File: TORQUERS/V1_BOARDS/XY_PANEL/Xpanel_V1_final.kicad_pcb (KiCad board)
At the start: 4 copper layers, 82.6 x 98 mm, 97 parts, among them J1 F3311A7H121014E200, J2 F3311A7H121014E200, Q1 BSS138, Q10 MBT2222ADW1T1, Q11 BSS138, Q12 MBT2222ADW1T1, Q2 BSS138, Q3 BSS138, Q4 MBT2222ADW1T1, Q5 BSS138, Q6 MBT2222ADW1T1, Q7 BSS138, Q8 BSS138, Q9 BSS138, U1 LTC3130EUDC-1-PBF, U2 DRV8830DGQ, U3 OPT4001DTST, U4 LTC3130EUDC-1-PBF

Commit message: made changes according to feedback
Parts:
- added locked: CL21A106KOQNNNE, AA_AUTO_LOADER:CAPC2012X140N, B.Cu at (147.0, 94.5)
- locked: renamed from R23; value 0 -> locked
- locked: renamed from Q7; value BSS138 -> locked
- locked: renamed from R18; value 10K -> locked
- locked: renamed from D7; value B220 -> locked
- locked: renamed from Q11; value BSS138 -> locked
- locked: renamed from C10; value 10nF -> locked
- locked: renamed from C13; value 10nF -> locked
- locked: renamed from R5; value 0 -> locked
- locked: renamed from U1; value LTC3130EUDC-1-PBF -> locked
- locked: renamed from R3; value 0 -> locked
- locked: renamed from D5; value B220 -> locked
- locked: renamed from R33; value 10K -> locked
- locked: renamed from R25; value 10K -> locked
- locked: renamed from C11; value 10nF -> locked
- locked: renamed from R31; value 10K -> locked
- locked: renamed from C12; value 10nF -> locked
- locked: renamed from JP4; value ~ -> locked
- locked: renamed from R29; value 10K -> locked
- locked: renamed from R37; value 10K -> locked
- locked: renamed from R38; value 100K -> locked
- locked: renamed from Q8; value BSS138 -> locked
- locked: renamed from R24; value 10K -> locked
- locked: renamed from R30; value 600 -> locked
- locked: renamed from R22; value 0 -> locked
- locked: renamed from R35; value 600 -> locked
- locked: renamed from R32; value 10K -> locked
- locked: renamed from R11; value 0 -> locked
- locked: renamed from R28; value 0 -> locked
- locked: renamed from R15; value 10K -> locked
- locked: renamed from R2; value 0 -> locked
- locked: renamed from Q9; value BSS138 -> locked
- locked: renamed from U4; value LTC3130EUDC-1-PBF -> locked
- locked: renamed from Q2; value BSS138 -> locked
- locked: renamed from Q3; value BSS138 -> locked
- locked: renamed from R27; value 0 -> locked
- locked: renamed from Q1; value BSS138 -> locked
- locked: renamed from R1; value 0 -> locked
- locked: renamed from D4; value B220 -> locked
- locked: renamed from R12; value 0 -> locked
- locked: renamed from R6; value 0 -> locked
- locked: renamed from R34; value 100K -> locked
- locked: renamed from D8; value B220 -> locked
- locked: renamed from JP3; value ~ -> locked
- locked: renamed from R10; value 0 -> locked
- locked: renamed from R21; value 600 -> locked
- locked: renamed from R4; value 0 -> locked
- locked: renamed from Q6; value MBT2222ADW1T1 -> locked
- locked: renamed from Q10; value MBT2222ADW1T1 -> locked
- locked: renamed from C6; value 10uF -> locked
- locked: renamed from R26; value 100K -> locked
- locked: renamed from Q5; value BSS138 -> locked
- locked: renamed from R7; value 0 -> locked
- locked: renamed from R36; value 10K -> locked
- locked: renamed from R16; value 600 -> locked
- locked: renamed from R17; value 10K -> locked
- locked: renamed from R19; value 10K -> locked
- locked: renamed from Q4; value MBT2222ADW1T1 -> locked
- locked: renamed from U2; value DRV8830DGQ -> locked
- locked: renamed from Q12; value MBT2222ADW1T1 -> locked
- locked: renamed from R20; value 100K -> locked
- locked: renamed from C8; value 0.1uF -> locked
- renumbered S1 to locked, R40 to locked, C19 to locked, L3 to locked, R9 to locked, C7 to locked, R8 to locked, C3 to locked, C17 to locked, R42 to locked, C15 to locked, J1 to locked, R13 to locked, C18 to locked, C1 to locked, R41 to locked, R39 to locked, L4 to locked, C16 to locked, C14 to locked, R14 to locked, C4 to locked, C9 to locked, C5 to locked
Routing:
- net Net-(D4-K): track 21.1 -> 23.7 mm
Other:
- board text added: "ARGUS_1 XY"
- board text added: "locked"
- board text removed: "XY SIDE PANEL BOARD ARGUS1 REV1.0"

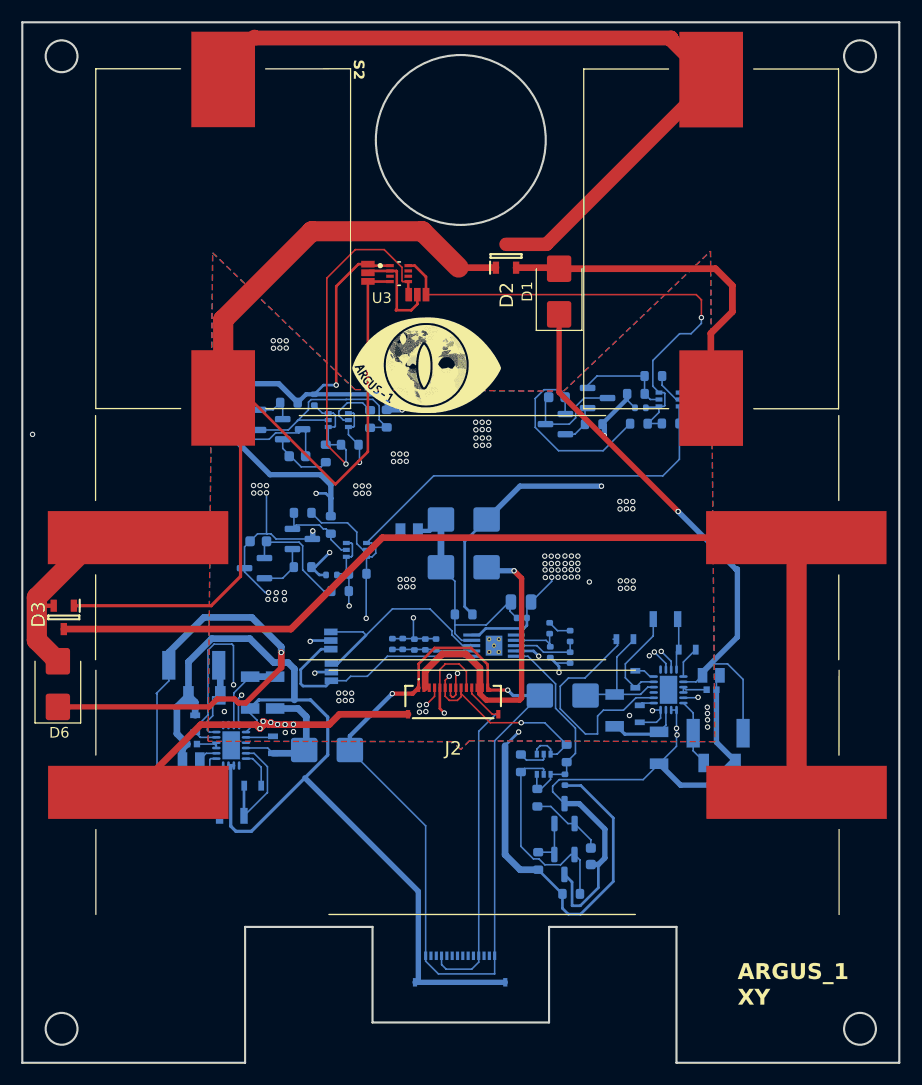
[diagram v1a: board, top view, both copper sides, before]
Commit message: added buck for coil driver
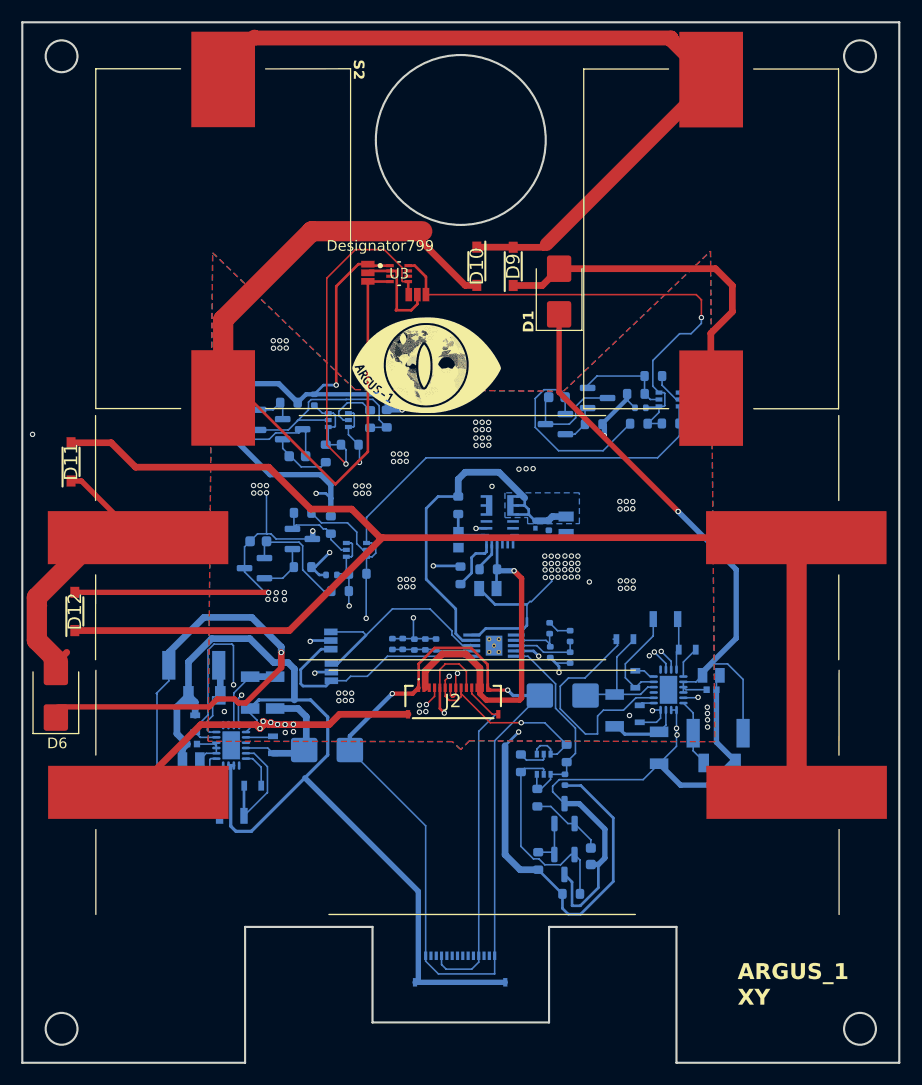
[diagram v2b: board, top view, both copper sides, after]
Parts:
- removed D2, D3: BAV99-TP, AA_AUTO_LOADER:SOT95P237X125-3N
- removed the locked at (152.2, 97.9)
- removed the locked at (152.2, 93.4)
- removed the locked at (152.1, 102.4)
- removed the locked at (157.5, 101.2)
- added C20: GRM033R60J224KE15D, AA_AUTO_LOADER:CAPC0603X33N, B.Cu at (158.9, 93.9)
- added C6: CL21A106KOQNNNE, AA_AUTO_LOADER:CAPC2012X140N, B.Cu at (154.4, 99.9)
- added D10: MBR0540-TP, AA_AUTO_LOADER:SOD3716X135N, F.Cu at (153.4, 69.6)
- added D11: MBR0540-TP, AA_AUTO_LOADER:SOD3716X135N, F.Cu at (115.2, 88.0)
- added D12: MBR0540-TP, AA_AUTO_LOADER:SOD3716X135N, F.Cu at (115.5, 102.1)
- added D9: MBR0540-TP, AA_AUTO_LOADER:SOD3716X135N, F.Cu at (156.8, 69.6)
- added IC1: MPM3610AGQV-Z, AA_AUTO_LOADER:MPM3610AGQVZ, B.Cu at (155.5, 93.4)
- added R12: 100K, Resistor_SMD:R_0603_1608Metric, B.Cu at (154.5, 98.1)
- added R43: 100K, Resistor_SMD:R_0603_1608Metric, B.Cu at (151.8, 98.7)
- added R44: 100K, Resistor_SMD:R_0603_1608Metric, B.Cu at (151.6, 92.1)
- added R45: RMCF0603FT19K1, AA_AUTO_LOADER:RESC1608X55N, B.Cu at (151.7, 95.3)
- moved locked 14.8 mm to (161.8, 94.0), turned to 90 degrees
- moved locked 9.09 mm to (160.2, 94.0), turned to -90 degrees
- moved D6 1.02 mm to (113.7, 109.9)
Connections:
- net Net-(D4-K) renamed 5V
- locked pad 1: Net-(U4-EXTVCC) -> GND
- locked pad 12: Net-(U1-EXTVCC) -> GND
- locked pad 3: Net-(U1-RUN) -> Net-(D1-K)
- locked pad 4: Net-(U1-RUN) -> Net-(D1-K)
- locked pad 2: Net-(U1-RUN) -> Net-(D1-K)
- locked pad 2: Net-(U4-RUN) -> Net-(D6-K)
- locked pad 12: Net-(U4-EXTVCC) -> GND
- locked pad 3: Net-(U4-RUN) -> Net-(D6-K)
- locked pad 4: Net-(U4-RUN) -> Net-(D6-K)
- locked pad 1: Net-(U1-EXTVCC) -> GND
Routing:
- net Net-(S3-Neg): track 96.6 -> 128.6 mm
- net +3.3V: track 207.0 -> 183.1 mm, vias 9 -> 8
- net Net-(U1-EXTVCC): track 22.3 -> 0.00 mm
- net GND: track 383.4 -> 399.2 mm, vias 116 -> 120
- net 5V: track 23.7 -> 35.8 mm
- net Net-(IC1-VCC): track 0.00 -> 9.06 mm, vias 0 -> 2
- net /solar_panel_electronics/7023_vout: track 22.3 -> 30.1 mm
- net Net-(IC1-PG): track 0.00 -> 5.22 mm
- net Net-(IC1-FB): track 0.00 -> 4.30 mm
- net Net-(D1-K): track 54.4 -> 57.5 mm
- net VBATT: track 30.9 -> 33.9 mm
- net Net-(D6-K): track 57.6 -> 60.5 mm
- net Net-(S1-Neg): track 77.0 -> 79.9 mm
- net Net-(U1-RUN): track 2.79 -> 0.00 mm
- net Net-(IC1-EN): track 0.00 -> 2.79 mm
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- added copper zone on B.Cu, net 5V

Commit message: made changes to the board
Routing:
- net GND: track 399.2 -> 421.0 mm, vias 120 -> 124
- net VSOLAR: track 84.9 -> 86.5 mm

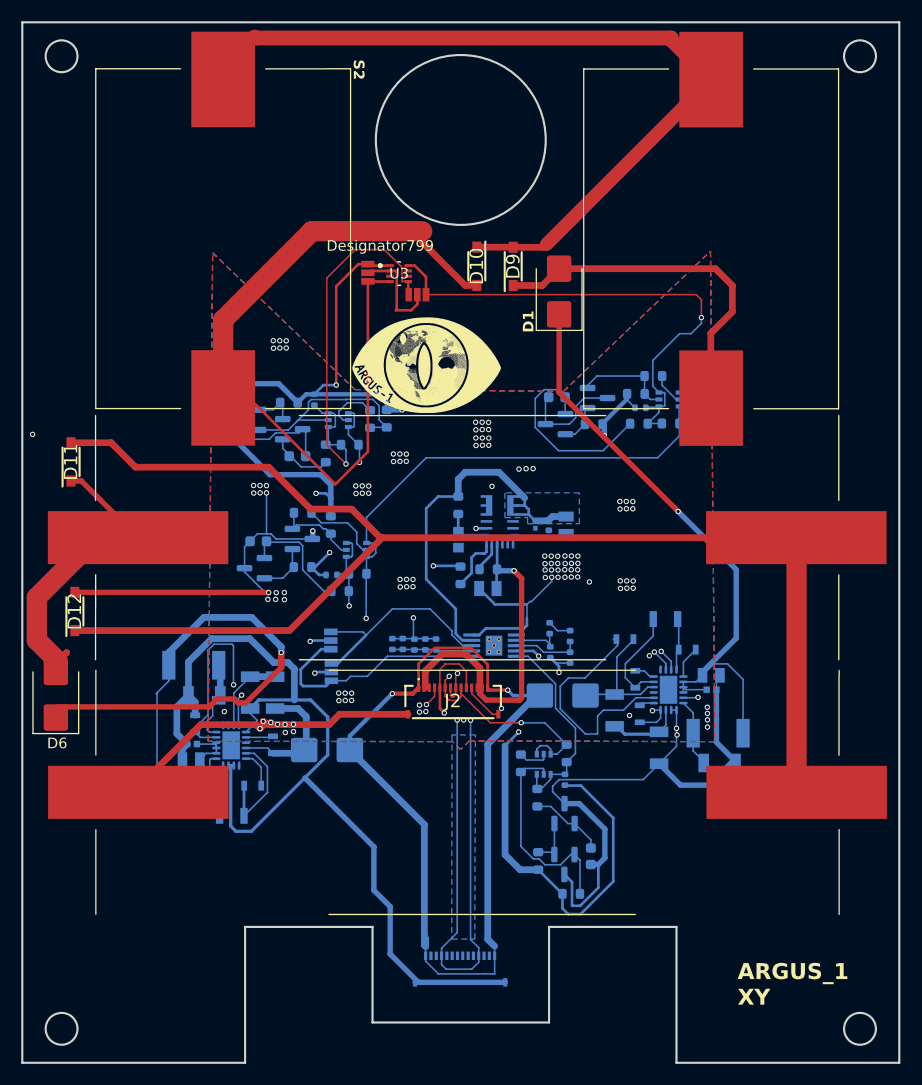
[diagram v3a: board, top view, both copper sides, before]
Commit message: final push XY board with step updated
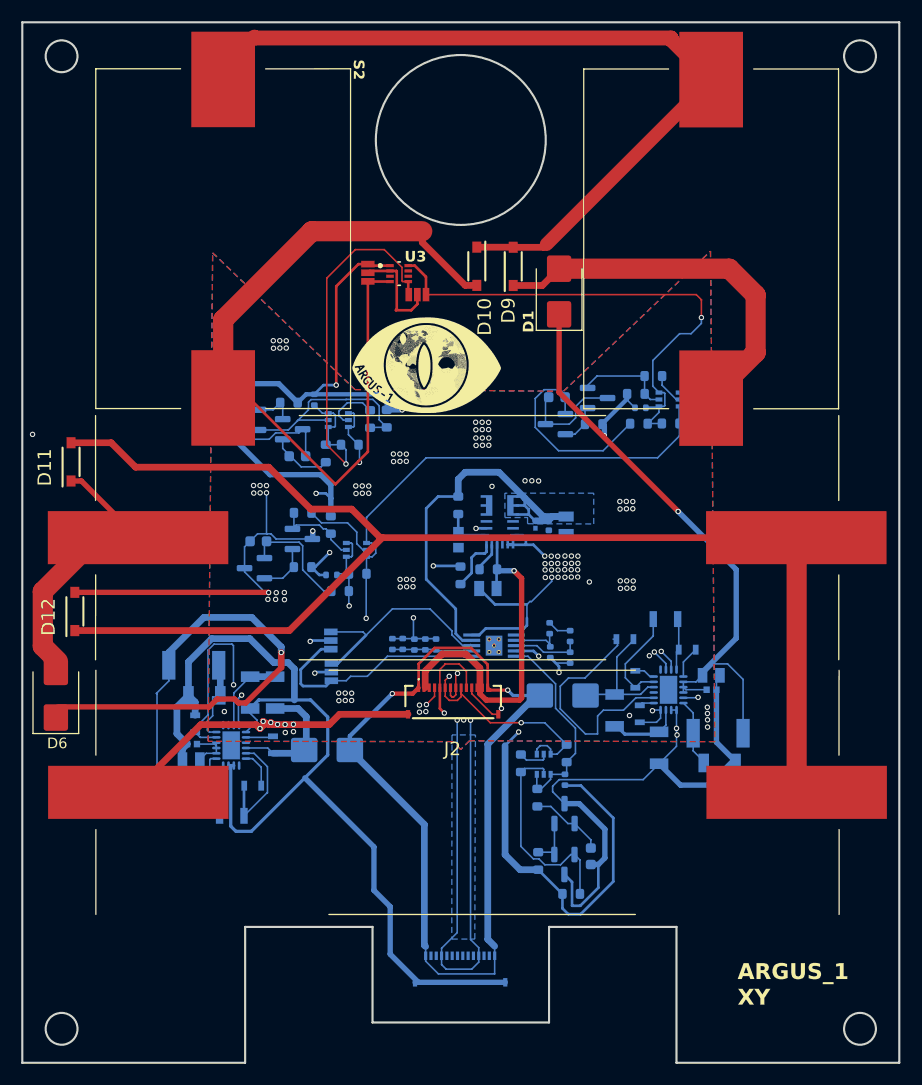
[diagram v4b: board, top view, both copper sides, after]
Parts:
- C10, C11, C12, C13: renamed from locked; value locked -> 10nF
- C8: renamed from locked; value locked -> 0.1uF
- D7, D8: renamed from locked; value locked -> B220
- JP3, JP4: renamed from locked; value locked -> ~
- Q1, Q11, Q2, Q3, Q5, Q7, Q8, Q9: renamed from locked; value locked -> BSS138
- Q10, Q12, Q4, Q6: renamed from locked; value locked -> MBT2222ADW1T1
- R1, R10, R11, R2, R22, R23, R27, R28, R3, R4, R5, R6, R7: renamed from locked; value locked -> 0
- R15, R17, R18, R19, R24, R25, R29, R31, R32, R33, R36, R37: renamed from locked; value locked -> 10K
- R16, R21, R30, R35: renamed from locked; value locked -> 600
- R20, R26, R34, R38: renamed from locked; value locked -> 100K
- U1, U4: renamed from locked; value locked -> LTC3130EUDC-1-PBF
- U2: renamed from locked; value locked -> DRV8830DGQ
- renumbered locked to C1, locked to C14, locked to C15, locked to C16, locked to C17, locked to C18, locked to C19, locked to C2, locked to C3, locked to C4, locked to C5, locked to C7, locked to C9, locked to J1, locked to L3, locked to L4, locked to R13, locked to R14, locked to R39, locked to R40, locked to R41, locked to R42, locked to R8, locked to R9, locked to S1
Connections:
- IC1 pad 21: unconnected-(IC1-SW_4-Pad21) -> /TORQUE_COIL/nc
- IC1 pad 4: unconnected-(IC1-SW_1-Pad4) -> /TORQUE_COIL/nc
- IC1 pad 5: unconnected-(IC1-SW_1-Pad4) -> /TORQUE_COIL/nc
- IC1 pad 6: unconnected-(IC1-SW_1-Pad4) -> /TORQUE_COIL/nc
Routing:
- net GND: track 421.0 -> 427.3 mm
- net 5V: track 35.8 -> 40.4 mm
- net /solar_panel_electronics/3224_vout: track 33.2 -> 36.1 mm
- net /solar_panel_electronics/7023_vout: track 30.1 -> 27.3 mm
- net VSOLAR: track 86.5 -> 85.6 mm
- net +3.3V: track 183.1 -> 183.6 mm
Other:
- board text added: "XY SIDE PANEL BOARD ARGUS1 REV1.0"
- board text removed: "locked"
